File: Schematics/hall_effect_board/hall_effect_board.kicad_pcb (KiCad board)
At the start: 2 copper layers, 17.5 x 30.5 mm, 5 parts, among them J1 B04B-PASK, U1 TMAG5273A1QDBVT

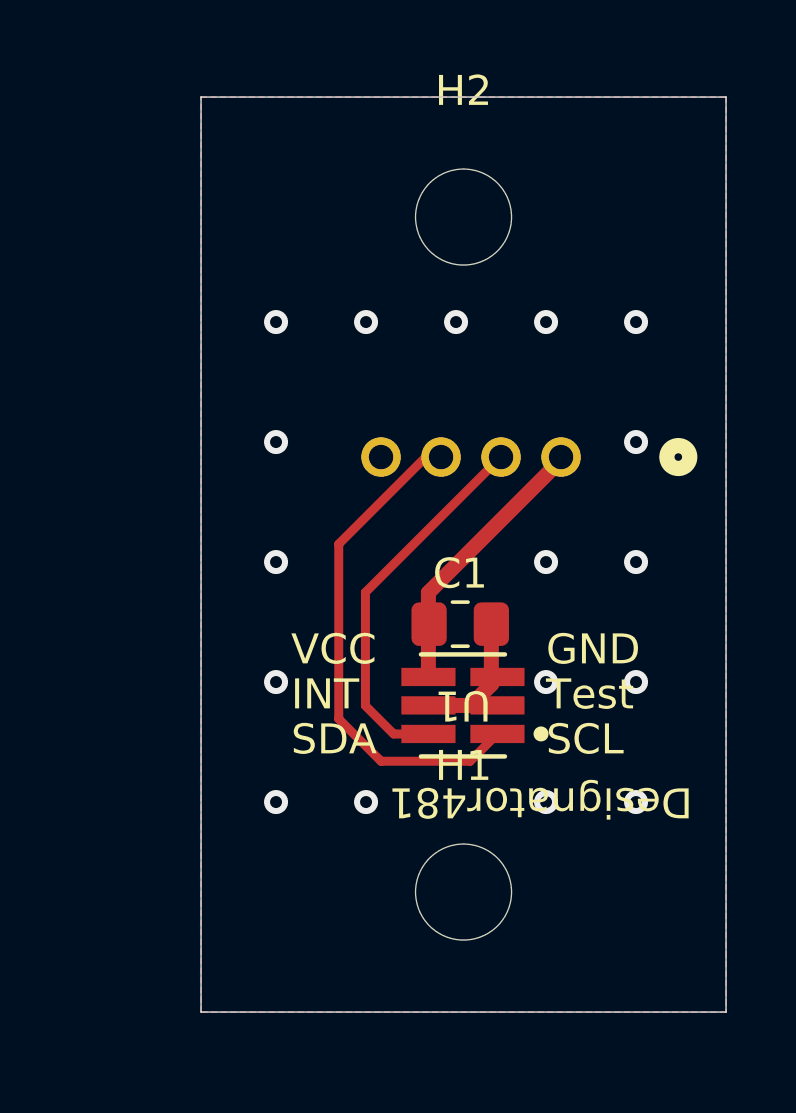
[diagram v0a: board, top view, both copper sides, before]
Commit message: cleaned up hall effect, switched to plated through holes
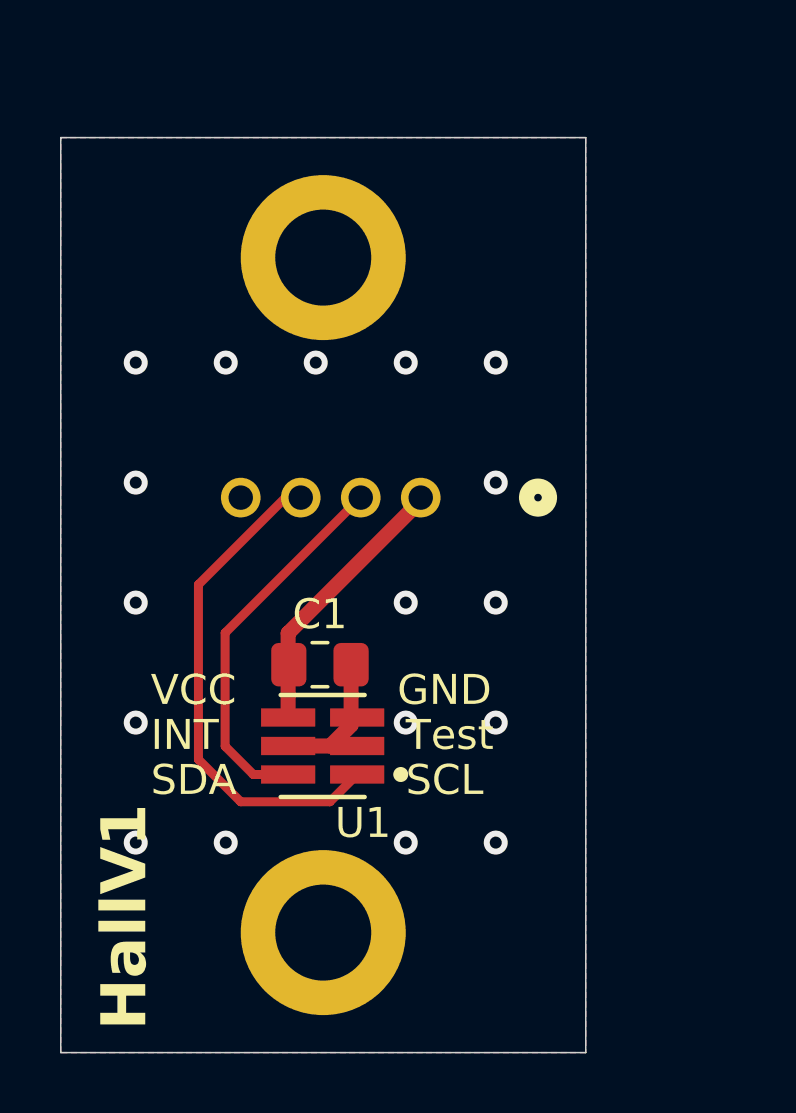
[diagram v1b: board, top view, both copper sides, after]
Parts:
- H1, H2: footprint MountingHole:MountingHole_3.2mm_M3 -> MountingHole:MountingHole_3.2mm_M3_ISO14580_Pad
- moved C1 4.87 mm to (120.0, 75.9)
- moved H2 4.87 mm to (120.1, 62.4)
- moved H1 4.87 mm to (120.1, 84.9)
- moved J1 4.87 mm to (123.3, 70.4)
- moved U1 4.87 mm to (120.1, 78.6)
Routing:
- net GND: vias 16 -> 17
- net (no net): vias 1 -> 0
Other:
- board text added: "Emily Ferraioli"
- board text added: "HallV1"
- board text added: "March 2026"

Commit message: update for emily!!
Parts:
- removed J1: B04B-PASK, footprints:CONN_B04B-PASK_JST
- added J3: HALL-1, footprints:CONN_SD-105309-100_04_MOL, B.Cu at (123.6, 67.8)
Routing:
- net SCL: track 12.9 -> 18.6 mm
- net +3V3: track 9.50 -> 11.8 mm
- net SCA: track 16.5 -> 15.1 mm

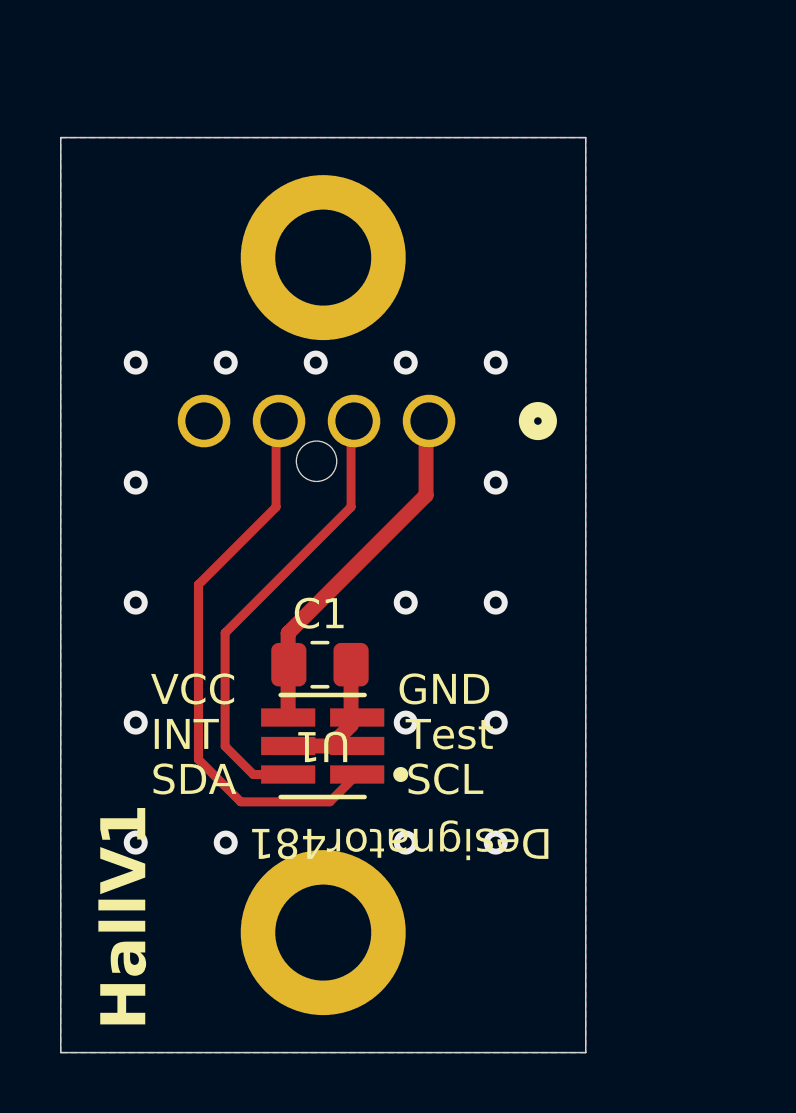
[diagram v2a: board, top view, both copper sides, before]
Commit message: Footprint Update
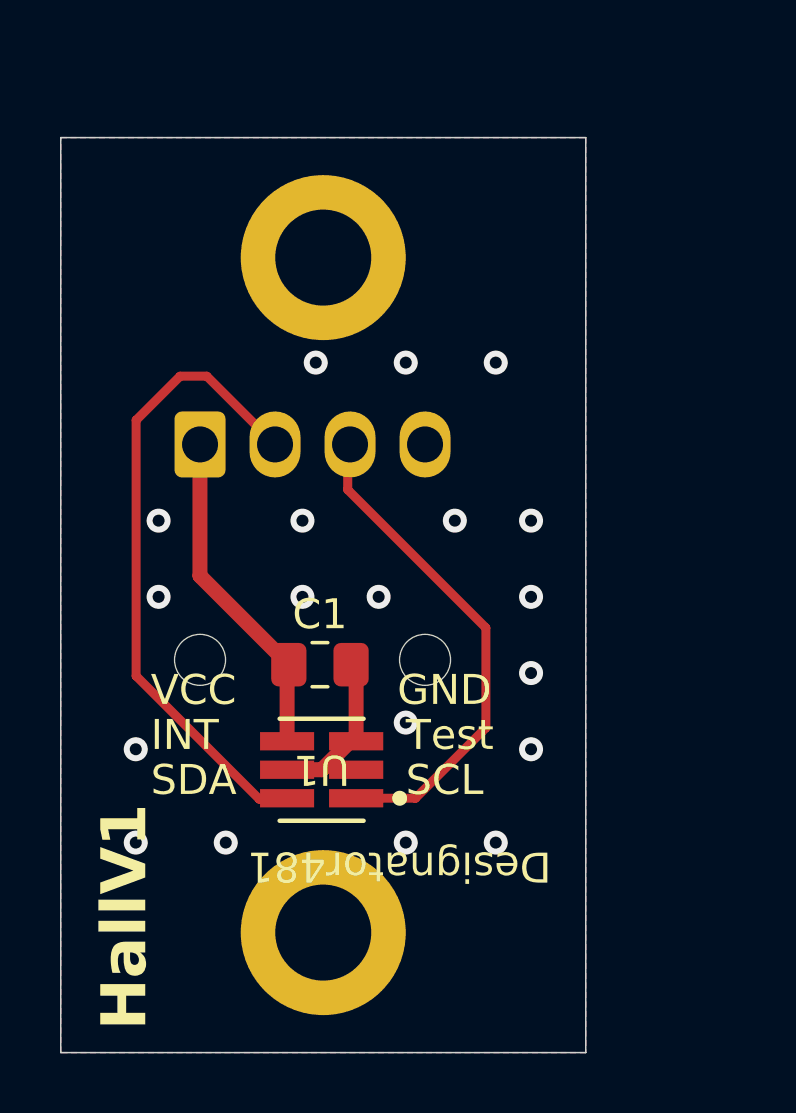
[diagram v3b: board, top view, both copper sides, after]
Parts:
- J3: footprint footprints:CONN_SD-105309-100_04_MOL -> Connector_Molex:Molex_Nano-Fit_105313-xx04_1x04_P2.50mm_Horizontal
- moved J3 7.67 mm to (116.0, 68.6), turned to -90 degrees
- moved U1 0.79 mm to (120.0, 79.4)
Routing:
- net SCA: track 15.1 -> 21.5 mm
- net SCL: track 18.6 -> 17.2 mm
- net GND: track 4.40 -> 5.20 mm, vias 17 -> 19

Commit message: Silkscreen update
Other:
- board text removed: "INT"
- board text removed: "Test"

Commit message: Add LED
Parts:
- removed J3: HALL-1, Connector_Molex:Molex_Nano-Fit_105313-xx04_1x04_P2.50mm_Horizontal
- added D1: PWR_3V3_LED (GRN), LED_SMD:LED_0603_1608Metric, F.Cu at (113.6, 61.4)
- added J1: HALL-1, Connector_Molex:Molex_Nano-Fit_105313-xx04_1x04_P2.50mm_Horizontal, B.Cu at (116.0, 68.5)
- added R1: 3.3k, Resistor_SMD:R_0603_1608Metric, F.Cu at (113.8, 64.9)
- moved H2 22.5 mm to (120.1, 84.8)
- moved H1 22.5 mm to (120.1, 62.4)
- moved C1 0.29 mm to (120.1, 76.1)
- moved U1 0.26 mm to (119.8, 79.4)
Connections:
- U1 pad 6: SCA -> SDA
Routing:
- net SDA: track 0.00 -> 29.2 mm
- net SCA: track 21.5 -> 0.00 mm
- net Net-(D1-A): track 0.00 -> 4.57 mm
- net SCL: track 17.2 -> 21.3 mm
- net +3V3: track 11.7 -> 15.3 mm

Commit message: Found issue on hall board, only effects LED
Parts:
- C1: value 0.01uF -> 10uF
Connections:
- D1 pad 1: Net-(D1-A) -> GND
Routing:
- net Net-(D1-A): track 4.57 -> 3.00 mm
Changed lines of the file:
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@@
 			)
 		)
-		(property "LCSC" "C2297"
+		(property "JLCSC" "C2297"
 			(at 0 0 -90)
 			(unlocked yes)
@@
 		)
 		(property ki_fp_filters "LED* LED_SMD:* LED_THT:*")
+		(sheetname "Root")
+		(sheetfile "hall_effect_board.kicad_sch")
 		(attr smd)
 		(fp_line
@@
 			(layers "F.Cu" "F.Paste" "F.Mask")
 			(roundrect_rratio 0.25)
-			(net 4 "Net-(D1-A)")
+			(net 1 "GND")
 			(pinfunction "K")
 			(pintype "passive")
@@
 		)
 		(property "Footprint" "footprints:DBV0006A-IPC_A"
-			(at 0 0 360)
+			(at 0 0 0)
 			(layer "F.Fab")
 			(hide yes)
@@
 		)
 		(property "Datasheet" "${KIPRJMOD}/../../Datasheets/tmag5273.pdf"
-			(at 0 0 360)
+			(at 0 0 0)
 			(layer "F.Fab")
 			(hide yes)
@@
 		)
 		(property "Description" ""
-			(at 0 0 360)
+			(at 0 0 0)
 			(layer "F.Fab")
 			(hide yes)
@@
 		)
 		(property ki_fp_filters "DBV0006A-IPC_A DBV0006A-IPC_B DBV0006A-IPC_C DBV0006A-MFG")
+		(sheetname "Root")
+		(sheetfile "hall_effect_board.kicad_sch")
 		(attr smd)
 		(fp_line
@@
 			)
 		)
-		(property "LCSC" "C22978"
+		(property "JLCSC" "C22978"
 			(at 0 0 0)
 			(unlocked yes)
@@
 		)
 		(property ki_fp_filters "R_*")
+		(sheetname "Root")
+		(sheetfile "hall_effect_board.kicad_sch")
 		(attr smd)
 		(fp_line
@@
 		)
 		(property ki_fp_filters "MountingHole*")
+		(sheetname "Root")
+		(sheetfile "hall_effect_board.kicad_sch")
 		(attr exclude_from_pos_files exclude_from_bom)
 		(fp_circle
@@
 		)
 		(property ki_fp_filters "MountingHole*")
+		(sheetname "Root")
+		(sheetfile "hall_effect_board.kicad_sch")
 		(attr exclude_from_pos_files exclude_from_bom)
 		(fp_circle
@@
 			)
 		)
-		(property "Value" "0.01uF"
+		(property "Value" "10uF"
 			(at 0 1.68 0)
 			(layer "F.Fab")
@@
 			)
 		)
-		(property "Digikey" "399-C0805X103K5RAC7210CT-ND"
+		(property "JLCSC" "C15850"
 			(at 0 0 0)
 			(unlocked yes)
@@
 		)
 		(property ki_fp_filters "C_*")
+		(sheetname "Root")
+		(sheetfile "hall_effect_board.kicad_sch")
 		(attr smd)
 		(fp_line
@@
 		)
 		(property ki_fp_filters "Connector*:*_1x??_*")
+		(sheetname "Root")
+		(sheetfile "hall_effect_board.kicad_sch")
 		(attr through_hole)
 		(fp_line
@@
 	)
 	(segment
+		(start 113.604226 64.296067)
+		(end 113.604226 62.200432)
+		(width 0.3)
+		(layer "F.Cu")
+		(net 4)
+	)
+	(segment
 		(start 112.965431 64.934862)
 		(end 113.604226 64.296067)
 		(width 0.3)
 		(layer "F.Cu")
-		(net 4)
-	)
-	(segment
-		(start 113.604226 64.296067)
-		(end 113.604226 60.625432)
-		(width 0.3)
-		(layer "F.Cu")
